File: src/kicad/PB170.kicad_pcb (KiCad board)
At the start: 4 copper layers, 96.5 x 71.1 mm, 37 parts, among them J1 USB_C_Receptacle_USB2.0-Conne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, J2 USB_B_Micro, Q1 P-MOSFET-MLP_HS, Q2 BC817, SW1 SW_MEC_5E, SW2 SW_MEC_5E, U1 74HC00, U2 74HC08, U3 74HC4511D, U4 HEF4518BT

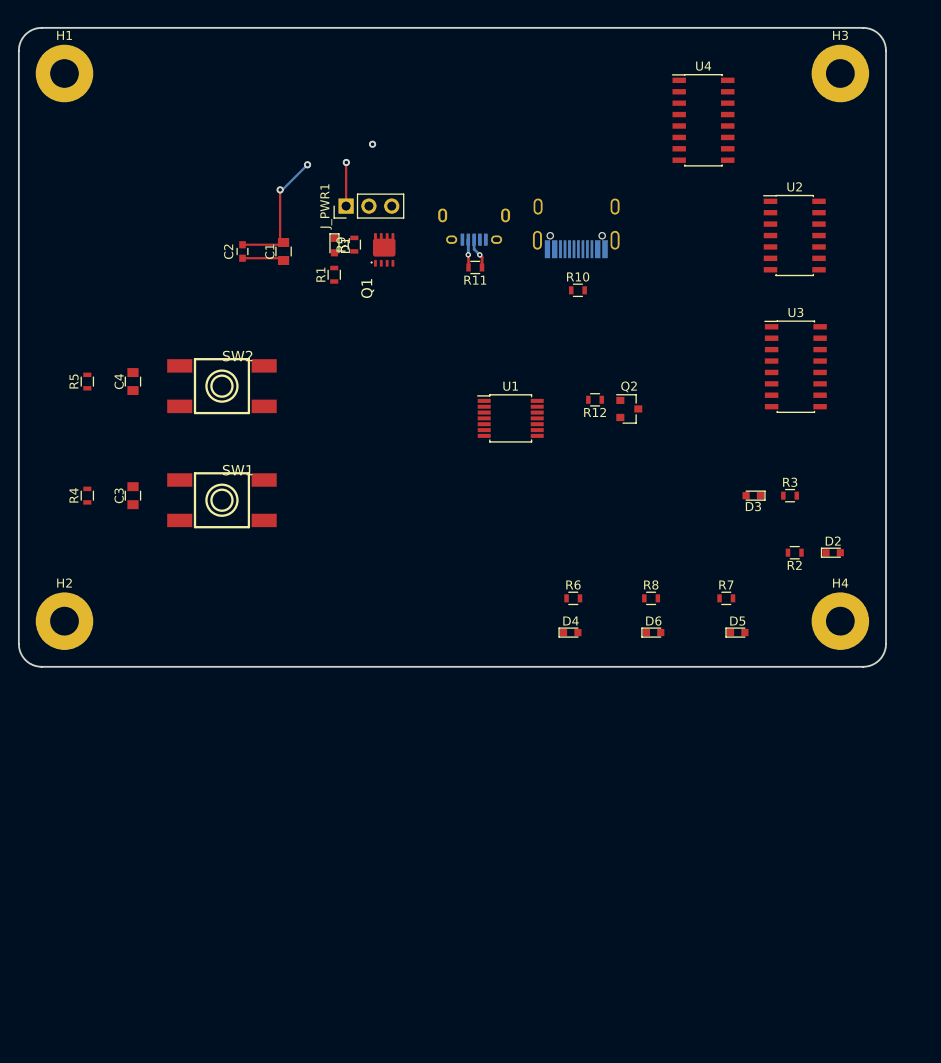
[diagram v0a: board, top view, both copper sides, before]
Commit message: added annotations, power connections to parts
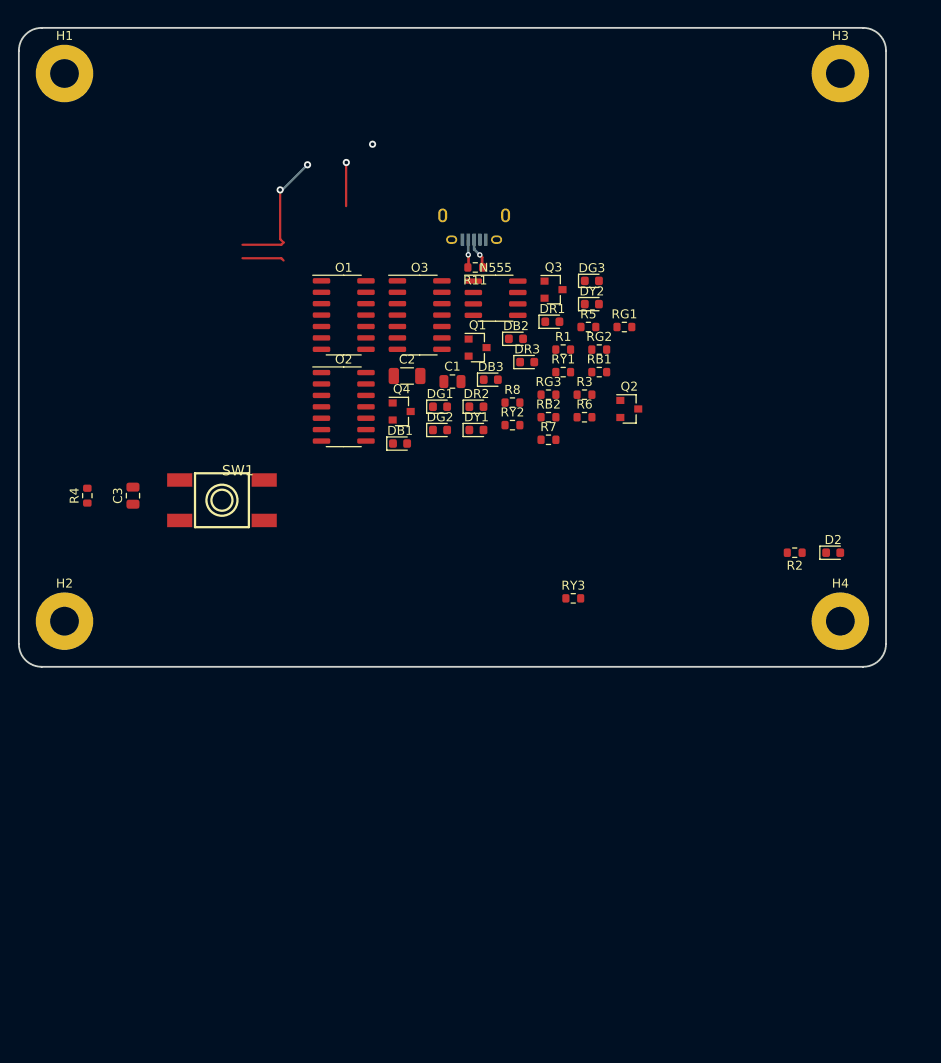
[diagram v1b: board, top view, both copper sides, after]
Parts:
- removed C4: 10uF, Capacitors_SMD:C_0805
- removed D1: LED red, LEDs:LED_0603
- removed D3: LED yellow, LEDs:LED_0603
- removed D4: LED green, LEDs:LED_0603
- removed D5: LED blue, LEDs:LED_0603
- removed D6: LED white, LEDs:LED_0603
- removed J1: USB_C_Receptacle_USB2.0-Connector, PB170:USB_C_Female-16Pin-HPJF
- removed J_PWR1: Conn_01x03, Pin_Headers:Pin_Header_Straight_1x03_Pitch2.54mm
- removed R10, R12: 220R, Resistors_SMD:R_0603
- removed R9: 10k, Resistors_SMD:R_0603
- removed SW2: SW_MEC_5E, PB170:TactileSwitch_C381064
- removed U1: 74HC00, Housings_SSOP:TSSOP-14_4.4x5mm_Pitch0.65mm
- removed U2: 74HC08, Housings_SOIC:SOIC-14_3.9x8.7mm_Pitch1.27mm
- removed U3: 74HC4511D, Housings_SOIC:SOIC-16_3.9x9.9mm_Pitch1.27mm
- removed U4: HEF4518BT, Housings_SOIC:SOIC-16_3.9x9.9mm_Pitch1.27mm
- added DB1: LED blue, LED_SMD:LED_0603_1608Metric, F.Cu at (83.1, 71.7)
- added DB2: LED blue, LED_SMD:LED_0603_1608Metric, F.Cu at (96.0, 60.0)
- added DB3: LED blue, LED_SMD:LED_0603_1608Metric, F.Cu at (93.2, 64.6)
- added DG1: LED green, LED_SMD:LED_0603_1608Metric, F.Cu at (87.5, 67.6)
- added DG2: LED green, LED_SMD:LED_0603_1608Metric, F.Cu at (87.5, 70.2)
- added DG3: LED green, LED_SMD:LED_0603_1608Metric, F.Cu at (104.4, 53.6)
- added DR1: LED red, LED_SMD:LED_0603_1608Metric, F.Cu at (100.0, 58.1)
- added DR2: LED red, LED_SMD:LED_0603_1608Metric, F.Cu at (91.6, 67.6)
- added DR3: LED red, LED_SMD:LED_0603_1608Metric, F.Cu at (97.2, 62.6)
- added DY1: LED yellow, LED_SMD:LED_0603_1608Metric, F.Cu at (91.6, 70.2)
- added DY2: LED yellow, LED_SMD:LED_0603_1608Metric, F.Cu at (104.4, 56.1)
- added N555: NE555D, Package_SO:SOIC-8_3.9x4.9mm_P1.27mm, F.Cu at (93.7, 55.5)
- added O1: 74HC32, Package_SO:SOIC-14_3.9x8.7mm_P1.27mm, F.Cu at (76.8, 57.4)
- added O2: 74HC32, Package_SO:SOIC-14_3.9x8.7mm_P1.27mm, F.Cu at (76.8, 67.6)
- added O3: 74HC32, Package_SO:SOIC-14_3.9x8.7mm_P1.27mm, F.Cu at (85.2, 57.4)
- added Q3: BC817, Package_TO_SOT_SMD:SOT-23, F.Cu at (100.2, 54.5)
- added Q4: BC817, Package_TO_SOT_SMD:SOT-23, F.Cu at (83.2, 68.1)
- added R6: 10kR, Resistor_SMD:R_0603_1608Metric, F.Cu at (103.6, 68.7)
- added RB1: 220R, Resistor_SMD:R_0603_1608Metric, F.Cu at (105.2, 63.7)
- added RB2: 220R, Resistor_SMD:R_0603_1608Metric, F.Cu at (99.6, 68.7)
- added RG1: 180R, Resistor_SMD:R_0603_1608Metric, F.Cu at (108.0, 58.7)
- added RG2: 180R, Resistor_SMD:R_0603_1608Metric, F.Cu at (105.2, 61.2)
- added RG3: 180R, Resistor_SMD:R_0603_1608Metric, F.Cu at (99.6, 66.2)
- added RY1: 180R, Resistor_SMD:R_0603_1608Metric, F.Cu at (101.2, 63.7)
- added RY2: 180R, Resistor_SMD:R_0603_1608Metric, F.Cu at (95.6, 69.6)
- C1: value 10uF -> 10nF; footprint Capacitors_SMD:C_0805 -> Capacitor_SMD:C_0805_2012Metric
- C2: value 100nF -> 47uF; footprint Capacitors_SMD:C_0603 -> Capacitor_SMD:C_1206_3216Metric
- C3: footprint Capacitors_SMD:C_0805 -> Capacitor_SMD:C_0805_2012Metric
- D2: footprint LEDs:LED_0603 -> LED_SMD:LED_0603_1608Metric
- Q1: value P-MOSFET-MLP_HS -> BC817; footprint PB170:MLP3.3X3.3_HS -> Package_TO_SOT_SMD:SOT-23
- Q2: footprint TO_SOT_Packages_SMD:SOT-23 -> Package_TO_SOT_SMD:SOT-23
- R1: value 220R -> 130R; footprint Resistors_SMD:R_0603 -> Resistor_SMD:R_0603_1608Metric
- R11, R2, R4: footprint Resistors_SMD:R_0603 -> Resistor_SMD:R_0603_1608Metric
- R3: value 180R -> 220R; footprint Resistors_SMD:R_0603 -> Resistor_SMD:R_0603_1608Metric
- R5: value 10k -> 180R; footprint Resistors_SMD:R_0603 -> Resistor_SMD:R_0603_1608Metric
- R7: value 220R -> 10kR; footprint Resistors_SMD:R_0603 -> Resistor_SMD:R_0603_1608Metric
- R8: value 130R -> 220R; footprint Resistors_SMD:R_0603 -> Resistor_SMD:R_0603_1608Metric
- RY3: renamed from R6; footprint Resistors_SMD:R_0603 -> Resistor_SMD:R_0603_1608Metric
- moved R5 56.1 mm to (104.0, 58.7), turned to 0 degrees
- moved R1 26.8 mm to (101.2, 61.2), turned to 0 degrees
- moved R8 26.7 mm to (95.6, 67.1)
- moved R7 26.5 mm to (99.6, 71.2)
- moved R3 25.5 mm to (103.6, 66.2)
- moved C1 23.7 mm to (88.9, 64.8), turned to 0 degrees
- moved C2 23.0 mm to (83.8, 64.2), turned to 0 degrees
- moved Q1 15.0 mm to (91.7, 61.0), turned to 0 degrees
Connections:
- C1 pad 1: +5V -> Net-(C1-Pad1)
- C2 pad 1: +5V -> Net-(C2-Pad1)
- C3 pad 1: /SheetXOR/IN_A -> Net-(C3-Pad1)
- C3 pad 2: +5V -> Net-(C3-Pad2)
- D2 pad 2: /SheetXOR/IN_A -> Net-(C3-Pad1)
- H1 pad 1: Net-(H1-Pad1) -> (no net)
- H2 pad 1: Net-(H2-Pad1) -> (no net)
- H3 pad 1: Net-(H3-Pad1) -> (no net)
- H4 pad 1: Net-(H4-Pad1) -> (no net)
- J2 pad 1: +5V -> (no net)
- J2 pad 4: Net-(J2-Pad4) -> (no net)
- Q1 pad 1: +5V -> Net-(O1-Pad3)
- Q1 pad 2: +5V -> Net-(DR1-Pad2)
- Q1 pad 3: +5V -> Net-(C3-Pad1)
- Q2 pad 3: +5V -> Net-(C3-Pad1)
- R1 pad 1: +5V -> Net-(DR1-Pad1)
- R1 pad 2: Net-(D1-Pad2) -> GND
- R4 pad 1: /SheetXOR/IN_A -> Net-(C3-Pad1)
- R5 pad 1: /SheetXOR/IN_B -> Net-(DR3-Pad1)
- R7 pad 1: Net-(D5-Pad1) -> Net-(C2-Pad1)
- R7 pad 2: GND -> Net-(N555-Pad7)
- RY3 pad 1: Net-(D4-Pad1) -> (no net)
- SW1 pad 1: +5V -> Net-(C3-Pad2)
- SW1 pad 2: +5V -> Net-(C3-Pad2)
- SW1 pad 3: /SheetXOR/IN_A -> Net-(C3-Pad1)
- SW1 pad 4: /SheetXOR/IN_A -> Net-(C3-Pad1)

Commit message: Hopefully finished eeschema, added inverters for rs flip flops
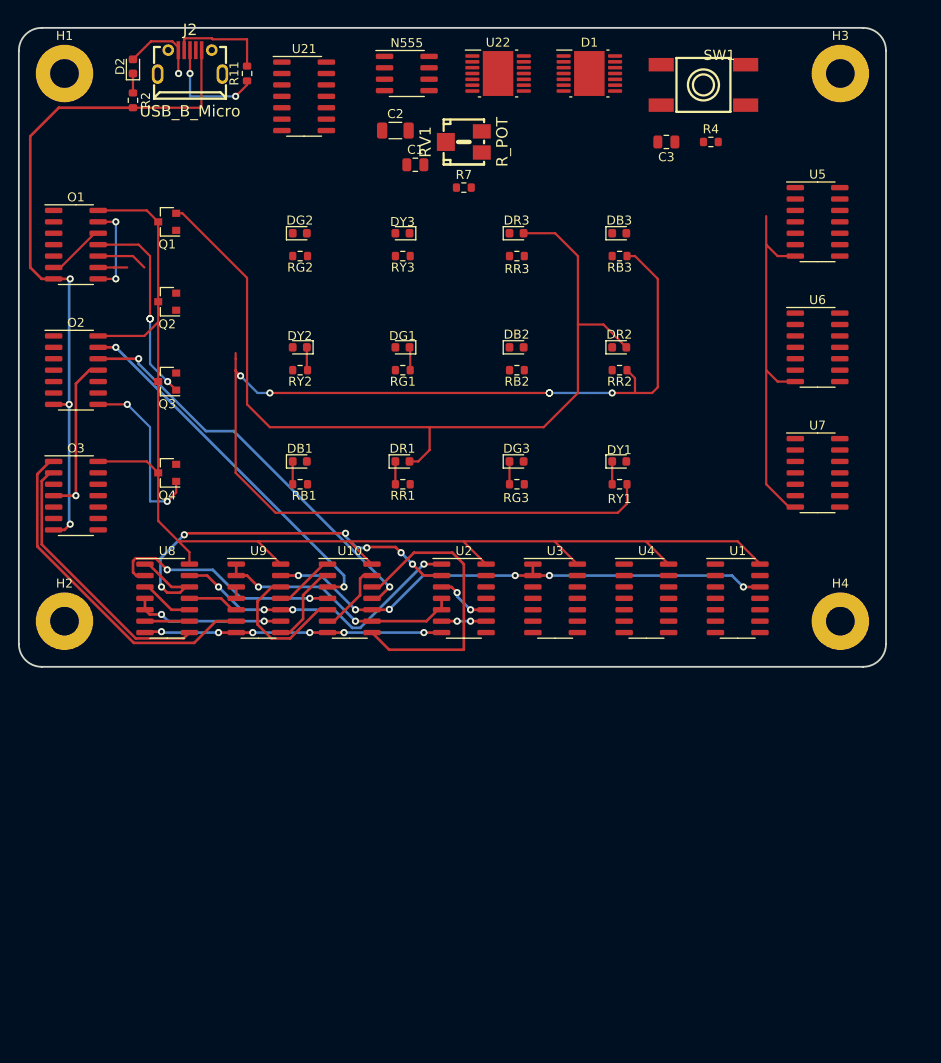
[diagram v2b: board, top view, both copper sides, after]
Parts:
- removed R1: 130R, Resistor_SMD:R_0603_1608Metric
- removed R3, R8: 220R, Resistor_SMD:R_0603_1608Metric
- removed R5: 180R, Resistor_SMD:R_0603_1608Metric
- removed R6: 10kR, Resistor_SMD:R_0603_1608Metric
- added D1: 74HC74, Package_SO:HTSSOP-14-1EP_4.4x5mm_P0.65mm_EP3.4x5mm_Mask3x3.1mm, F.Cu at (104.1, 30.5)
- added DY3: LED yellow, LED_SMD:LED_0603_1608Metric, F.Cu at (83.3, 48.3)
- added RB3: 220R, Resistor_SMD:R_0603_1608Metric, F.Cu at (107.5, 50.8)
- added RR1: 130R, Resistor_SMD:R_0603_1608Metric, F.Cu at (83.4, 76.2)
- added RR2: 220R, Resistor_SMD:R_0603_1608Metric, F.Cu at (107.5, 63.5)
- added RR3: 180R, Resistor_SMD:R_0603_1608Metric, F.Cu at (96.1, 50.8)
- added RV1: R_POT, PB170:potentiometer10k, F.Cu at (90.2, 38.1)
- added U1: 74HC08, Package_SO:SOIC-14_3.9x8.7mm_P1.27mm, F.Cu at (120.7, 88.9)
- added U10: 74HC08, Package_SO:SOIC-14_3.9x8.7mm_P1.27mm, F.Cu at (77.5, 88.9)
- added U2: 74HC08, Package_SO:SOIC-14_3.9x8.7mm_P1.27mm, F.Cu at (90.2, 88.9)
- added U21: 74HC08, Package_SO:SOIC-14_3.9x8.7mm_P1.27mm, F.Cu at (72.4, 33.0)
- added U22: 74HC74, Package_SO:HTSSOP-14-1EP_4.4x5mm_P0.65mm_EP3.4x5mm_Mask3x3.1mm, F.Cu at (94.0, 30.5)
- added U3: 74HC08, Package_SO:SOIC-14_3.9x8.7mm_P1.27mm, F.Cu at (100.3, 88.9)
- added U4: 74HC08, Package_SO:SOIC-14_3.9x8.7mm_P1.27mm, F.Cu at (110.5, 88.9)
- added U5: 74HC08, Package_SO:SOIC-14_3.9x8.7mm_P1.27mm, F.Cu at (129.5, 47.0)
- added U6: 74HC08, Package_SO:SOIC-14_3.9x8.7mm_P1.27mm, F.Cu at (129.5, 61.0)
- added U7: 74HC08, Package_SO:SOIC-14_3.9x8.7mm_P1.27mm, F.Cu at (129.5, 74.9)
- added U8: 74HC08, Package_SO:SOIC-14_3.9x8.7mm_P1.27mm, F.Cu at (57.1, 88.9)
- added U9: 74HC08, Package_SO:SOIC-14_3.9x8.7mm_P1.27mm, F.Cu at (67.3, 88.9)
- J2: footprint Connectors:USB_Micro-B -> PB170:MICRO-USB-SMD_MICROXNJ; moved to F.Cu
- moved D2 94.9 mm to (53.3, 29.7), turned to 90 degrees
- moved R2 89.2 mm to (53.3, 33.5), turned to 270 degrees
- moved R4 79.8 mm to (117.7, 38.1), turned to 0 degrees
- moved C3 71.2 mm to (112.7, 38.1), turned to 180 degrees
- moved SW1 70.8 mm to (116.8, 31.8)
- moved Q2 52.8 mm to (57.1, 55.9), turned to 180 degrees
- moved Q3 44.2 mm to (57.1, 64.8), turned to 180 degrees
- moved O3 43.2 mm to (47.0, 77.5)
- moved RY3 42.6 mm to (83.4, 50.8)
- moved Q1 37.3 mm to (57.1, 47.0), turned to 180 degrees
- moved J2 36.6 mm to (59.7, 29.2)
- moved RB1 35.6 mm to (71.9, 76.2)
- moved RG2 34.9 mm to (71.9, 50.8)
- moved R11 33.3 mm to (66.0, 30.5), turned to 90 degrees
- moved DY2 32.9 mm to (71.9, 61.0), turned to 180 degrees
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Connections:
- C3 pad 1: Net-(C3-Pad1) -> /blue/VCC
- D2 pad 2: Net-(C3-Pad1) -> /blue/VCC
- J2 pad 1: (no net) -> /blue/VCC
- N555 pad 3: (no net) -> 555output
- N555 pad 4: Net-(C3-Pad1) -> /blue/VCC
- N555 pad 8: Net-(C3-Pad1) -> /blue/VCC
- O1 pad 1: (no net) -> /red/r2
- O1 pad 10: (no net) -> /green/g1
- O1 pad 14: (no net) -> /blue/VCC
- O1 pad 2: (no net) -> /red/r1
- O1 pad 4: (no net) -> /green/g4
- O1 pad 5: (no net) -> /green/g3
- O1 pad 7: (no net) -> GND
- O1 pad 9: (no net) -> /green/g2
- O2 pad 1: (no net) -> /blue/b4
- O2 pad 12: (no net) -> /yellow/y4
- O2 pad 13: (no net) -> /yellow/y3
- O2 pad 14: (no net) -> /blue/VCC
- O2 pad 2: (no net) -> /blue/b3
- O2 pad 4: (no net) -> /blue/b2
- O2 pad 5: (no net) -> /blue/b1
- O2 pad 7: (no net) -> GND
- O3 pad 1: (no net) -> /yellow/y2
- O3 pad 10: (no net) -> Net-(O3-Pad10)
- O3 pad 14: (no net) -> /blue/VCC
- O3 pad 2: (no net) -> /yellow/y1
- O3 pad 7: (no net) -> GND
- O3 pad 8: (no net) -> Net-(D1-Pad2)
- O3 pad 9: (no net) -> Net-(O3-Pad9)
- Q1 pad 3: Net-(C3-Pad1) -> /blue/VCC
- Q2 pad 3: Net-(C3-Pad1) -> /blue/VCC
- Q3 pad 3: Net-(C3-Pad1) -> /blue/VCC
- Q4 pad 3: Net-(C3-Pad1) -> /blue/VCC
- R4 pad 1: Net-(C3-Pad1) -> /blue/VCC
- RY3 pad 1: (no net) -> Net-(DY3-Pad1)
- SW1 pad 3: Net-(C3-Pad1) -> /blue/VCC
- SW1 pad 4: Net-(C3-Pad1) -> /blue/VCC
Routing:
- net GND: track 32.0 -> 281.5 mm, vias 4 -> 15
- net /blue/VCC: track 0.00 -> 153.9 mm, vias 0 -> 1
- net Net-(DR1-Pad2): track 0.00 -> 98.5 mm
- net D1Q: track 0.00 -> 58.4 mm, vias 0 -> 6
- net JK2Q: track 0.00 -> 47.5 mm, vias 0 -> 6
- net /yellow/y4: track 0.00 -> 45.9 mm, vias 0 -> 2
- net /yellow/y3: track 0.00 -> 41.0 mm, vias 0 -> 2
- net /yellow/y2: track 0.00 -> 38.1 mm
- net JK1!Q: track 0.00 -> 33.4 mm, vias 0 -> 4
- net Net-(U10-Pad12): track 0.00 -> 32.9 mm
- net /yellow/y1: track 0.00 -> 29.8 mm
- net D2!Q: track 0.00 -> 28.1 mm, vias 0 -> 2
- net JK1Q: track 0.00 -> 26.4 mm, vias 0 -> 2
- net Net-(O1-Pad11): track 0.00 -> 22.4 mm, vias 0 -> 4
- net Net-(O2-Pad8): track 0.00 -> 19.6 mm, vias 0 -> 2
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
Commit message: removed connections from pcbnew - restarting..
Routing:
- net GND: track 281.5 -> 14.0 mm, vias 15 -> 0
- net /blue/VCC: track 153.9 -> 9.09 mm
- net Net-(DR1-Pad2): track 98.5 -> 0.00 mm
- net D1Q: track 58.4 -> 1.33 mm, vias 6 -> 0
- net JK2Q: track 47.5 -> 0.00 mm, vias 6 -> 0
- net /yellow/y4: track 45.9 -> 0.07 mm, vias 2 -> 0
- net /yellow/y3: track 41.0 -> 0.00 mm, vias 2 -> 0
- net /yellow/y2: track 38.1 -> 0.00 mm
- net JK1!Q: track 33.4 -> 0.00 mm, vias 4 -> 0
- net Net-(U10-Pad12): track 32.9 -> 0.00 mm
- net /yellow/y1: track 29.8 -> 0.00 mm
- net JK1Q: track 26.4 -> 0.06 mm, vias 2 -> 0
- net D2!Q: track 28.1 -> 2.61 mm, vias 2 -> 0
- net Net-(O1-Pad11): track 22.4 -> 0.00 mm, vias 4 -> 0
- net Net-(O2-Pad8): track 19.6 -> 0.00 mm, vias 2 -> 0
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
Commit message: routing finished
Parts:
- added Inverter1: 74HC04, Package_SO:SOIC-14_3.9x8.7mm_P1.27mm, F.Cu at (95.0, 62.5)
- moved H1 135.6 mm to (135.0, 132.5)
- moved Q1 105.6 mm to (122.5, 130.0), turned to 0 degrees
- moved O3 97.9 mm to (136.3, 117.5)
- moved Q2 88.1 mm to (122.5, 115.0), turned to 0 degrees
- moved U8 80.8 mm to (136.3, 105.0)
- moved H4 76.5 mm to (67.5, 132.5)
- moved O1 76.0 mm to (107.5, 95.5)
- moved U9 69.2 mm to (136.4, 92.5)
- moved DB1 62.8 mm to (91.5, 133.4)
- moved RG2 62.8 mm to (91.5, 110.5)
- moved RY2 62.8 mm to (91.5, 123.2)
- moved DG2 62.8 mm to (91.5, 108.0)
- moved DY2 62.8 mm to (91.5, 120.7)
- moved RB1 62.8 mm to (91.5, 135.9)
- moved RG1 61.5 mm to (97.9, 123.2)
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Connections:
- U21 pad 11: Net-(U21-Pad11) -> Net-(Inverter1-Pad9)
- U21 pad 3: Net-(U21-Pad3) -> Net-(Inverter1-Pad1)
- U21 pad 4: JK1Q -> /blue/VCC
- U21 pad 5: /blue/VCC -> JK1Q
- U21 pad 6: Net-(U21-Pad6) -> Net-(Inverter1-Pad3)
- U21 pad 8: Net-(U21-Pad8) -> Net-(Inverter1-Pad5)
- U22 pad 1: Net-(U21-Pad6) -> Net-(Inverter1-Pad4)
- U22 pad 10: Net-(U21-Pad8) -> Net-(Inverter1-Pad6)
- U22 pad 13: Net-(U21-Pad11) -> Net-(Inverter1-Pad8)
- U22 pad 4: Net-(U21-Pad3) -> Net-(Inverter1-Pad2)
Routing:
- net GND: track 14.0 -> 551.1 mm, vias 0 -> 16
- net /blue/VCC: track 9.09 -> 483.4 mm, vias 1 -> 9
- net D2!Q: track 2.61 -> 204.2 mm, vias 0 -> 5
- net D2Q: track 0.00 -> 190.7 mm, vias 0 -> 5
- net JK2Q: track 0.00 -> 183.2 mm, vias 0 -> 6
- net JK1!Q: track 0.00 -> 175.1 mm, vias 0 -> 6
- net D1Q: track 1.33 -> 159.6 mm, vias 0 -> 5
- net JK1Q: track 0.06 -> 151.0 mm, vias 0 -> 5
- net JK2!Q: track 0.00 -> 123.3 mm, vias 0 -> 5
- net D1!Q: track 0.00 -> 118.5 mm
- net 555output: track 0.00 -> 104.0 mm, vias 0 -> 4
- net Net-(D1-Pad2): track 0.00 -> 70.7 mm, vias 0 -> 2
- net Net-(O3-Pad9): track 0.00 -> 70.0 mm, vias 0 -> 2
- net Net-(O3-Pad10): track 0.00 -> 70.0 mm, vias 0 -> 2
- net Net-(DY1-Pad2): track 0.00 -> 64.6 mm, vias 0 -> 3
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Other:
- board outline removed

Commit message: resolved push colisions
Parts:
- RR1: value 130R -> 220R
- RR3: value 180R -> 220R
- moved RR3 0.33 mm to (105.6, 110.2)
- moved RR1 0.09 mm to (97.9, 135.9)

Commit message: Corrected negations
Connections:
- net D1!Q renamed D1~Q
- net D2!Q renamed D2~Q
- net JK1!Q renamed JK1~Q
- net JK2!Q renamed JK2~Q
- H1 pad 1: (no net) -> Net-(H1-Pad1)
- H2 pad 1: (no net) -> Net-(H2-Pad1)
- H3 pad 1: (no net) -> Net-(H3-Pad1)
- H4 pad 1: (no net) -> Net-(H4-Pad1)
- J2 pad 4: (no net) -> Net-(J2-Pad4)
